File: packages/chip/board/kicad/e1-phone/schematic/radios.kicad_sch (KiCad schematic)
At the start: 0 parts

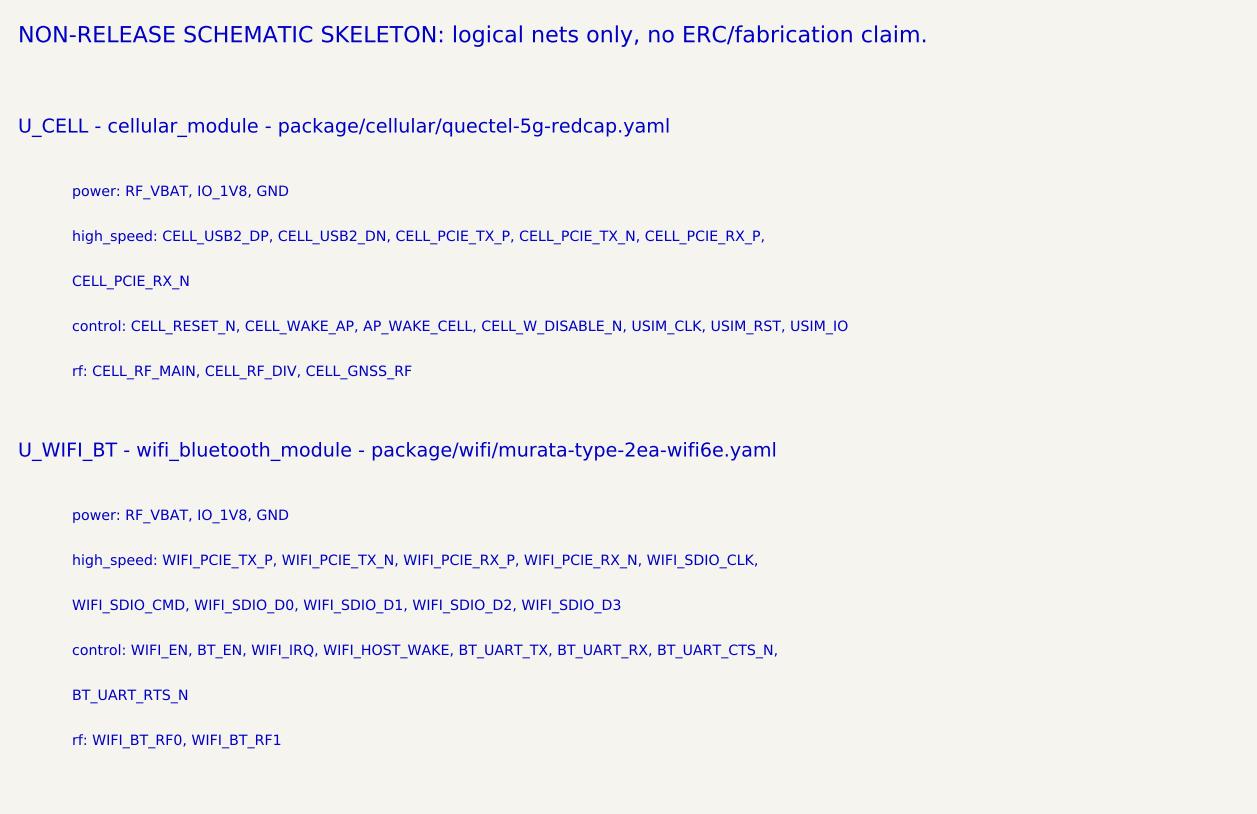
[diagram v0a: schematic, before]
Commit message: Prepare chip package for publishing
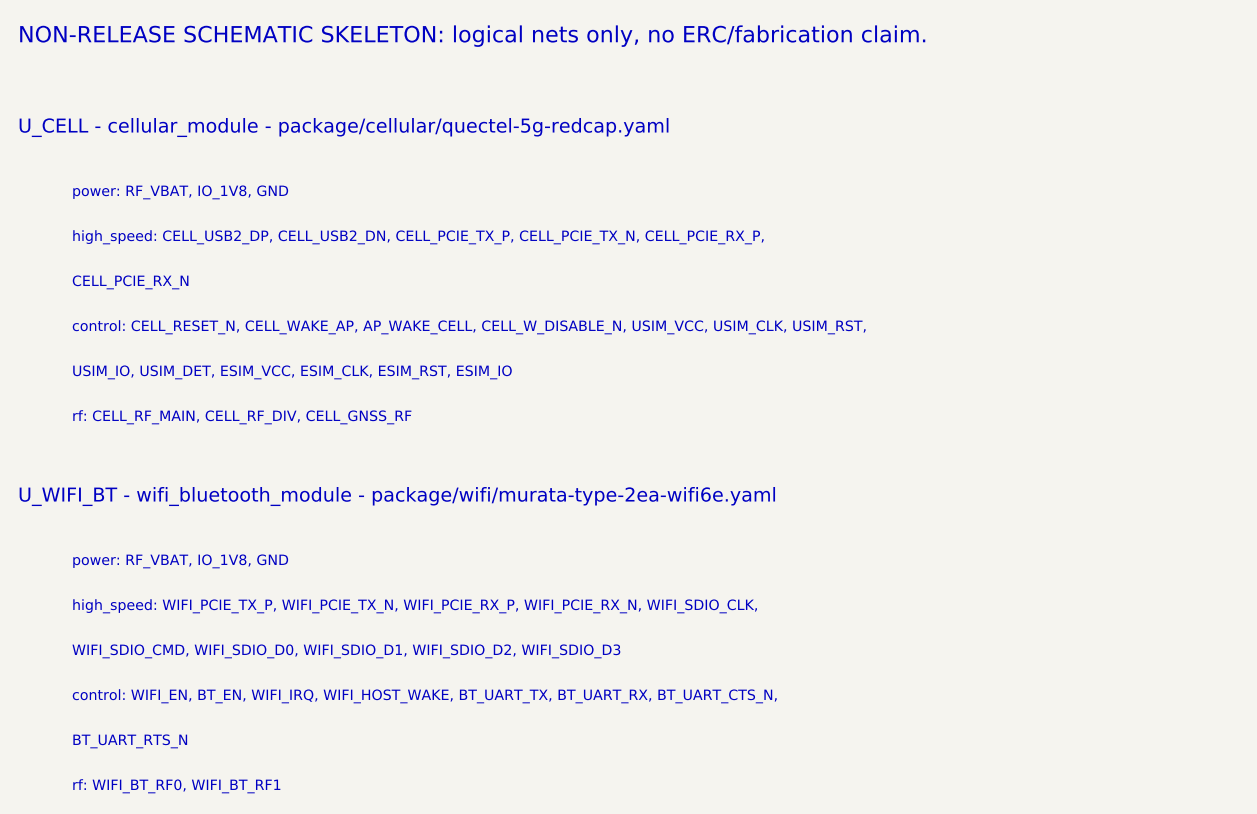
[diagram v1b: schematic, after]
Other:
- note added: "USIM_IO, USIM_DET, ESIM_VCC, ESIM_CLK, ESIM_RST, ESIM_IO"
- note added: "control: CELL_RESET_N, CELL_WAKE_AP, AP_WAKE_CELL, CELL_W_DISABLE_N, USIM_VCC, USIM_CLK, USIM_RST,"
- note removed: "control: CELL_RESET_N, CELL_WAKE_AP, AP_WAKE_CELL, CELL_W_DISABLE_N, USIM_CLK, USIM_RST, USIM_IO"
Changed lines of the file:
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@@
     (effects (font (size 1.15 1.15)) (justify left bottom))
   )
-  (text "control: CELL_RESET_N, CELL_WAKE_AP, AP_WAKE_CELL, CELL_W_DISABLE_N, USIM_CLK, USIM_RST, USIM_IO" (at 26.00 52.00 0)
+  (text "control: CELL_RESET_N, CELL_WAKE_AP, AP_WAKE_CELL, CELL_W_DISABLE_N, USIM_VCC, USIM_CLK, USIM_RST," (at 26.00 52.00 0)
     (effects (font (size 1.15 1.15)) (justify left bottom))
   )
-  (text "rf: CELL_RF_MAIN, CELL_RF_DIV, CELL_GNSS_RF" (at 26.00 57.00 0)
+  (text "USIM_IO, USIM_DET, ESIM_VCC, ESIM_CLK, ESIM_RST, ESIM_IO" (at 26.00 57.00 0)
     (effects (font (size 1.15 1.15)) (justify left bottom))
   )
-  (text "U_WIFI_BT - wifi_bluetooth_module - package/wifi/murata-type-2ea-wifi6e.yaml" (at 20.00 66.00 0)
+  (text "rf: CELL_RF_MAIN, CELL_RF_DIV, CELL_GNSS_RF" (at 26.00 62.00 0)
+    (effects (font (size 1.15 1.15)) (justify left bottom))
+  )
+  (text "U_WIFI_BT - wifi_bluetooth_module - package/wifi/murata-type-2ea-wifi6e.yaml" (at 20.00 71.00 0)
     (effects (font (size 1.55 1.55)) (justify left bottom))
   )
-  (text "power: RF_VBAT, IO_1V8, GND" (at 26.00 73.00 0)
+  (text "power: RF_VBAT, IO_1V8, GND" (at 26.00 78.00 0)
     (effects (font (size 1.15 1.15)) (justify left bottom))
   )
-  (text "high_speed: WIFI_PCIE_TX_P, WIFI_PCIE_TX_N, WIFI_PCIE_RX_P, WIFI_PCIE_RX_N, WIFI_SDIO_CLK," (at 26.00 78.00 0)
+  (text "high_speed: WIFI_PCIE_TX_P, WIFI_PCIE_TX_N, WIFI_PCIE_RX_P, WIFI_PCIE_RX_N, WIFI_SDIO_CLK," (at 26.00 83.00 0)
     (effects (font (size 1.15 1.15)) (justify left bottom))
   )
-  (text "WIFI_SDIO_CMD, WIFI_SDIO_D0, WIFI_SDIO_D1, WIFI_SDIO_D2, WIFI_SDIO_D3" (at 26.00 83.00 0)
+  (text "WIFI_SDIO_CMD, WIFI_SDIO_D0, WIFI_SDIO_D1, WIFI_SDIO_D2, WIFI_SDIO_D3" (at 26.00 88.00 0)
     (effects (font (size 1.15 1.15)) (justify left bottom))
   )
-  (text "control: WIFI_EN, BT_EN, WIFI_IRQ, WIFI_HOST_WAKE, BT_UART_TX, BT_UART_RX, BT_UART_CTS_N," (at 26.00 88.00 0)
+  (text "control: WIFI_EN, BT_EN, WIFI_IRQ, WIFI_HOST_WAKE, BT_UART_TX, BT_UART_RX, BT_UART_CTS_N," (at 26.00 93.00 0)
     (effects (font (size 1.15 1.15)) (justify left bottom))
   )
-  (text "BT_UART_RTS_N" (at 26.00 93.00 0)
+  (text "BT_UART_RTS_N" (at 26.00 98.00 0)
     (effects (font (size 1.15 1.15)) (justify left bottom))
   )
-  (text "rf: WIFI_BT_RF0, WIFI_BT_RF1" (at 26.00 98.00 0)
+  (text "rf: WIFI_BT_RF0, WIFI_BT_RF1" (at 26.00 103.00 0)
     (effects (font (size 1.15 1.15)) (justify left bottom))
   )
